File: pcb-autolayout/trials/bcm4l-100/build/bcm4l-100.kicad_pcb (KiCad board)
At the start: 4 copper layers, 80 x 60 mm, 120 parts, among them J1 MicroFit 2x4, J2 MicroFit 2x6, J3 SWD, Q1 SQD40P06 (P-MOS), Q11 AO3401A, Q12 MMBT3904, Q13 AO3401A, Q14 MMBT3904, Q15 AO3401A, Q16 MMBT3904, Q17 AO3401A, Q18 MMBT3904, SW1 RESET, U1 TPS54202, U2 AMS1117-3.3, U3 TJA1051T/3, U4 TJA1021T/20, U5 STM32F103C8T6, Y1 8MHz

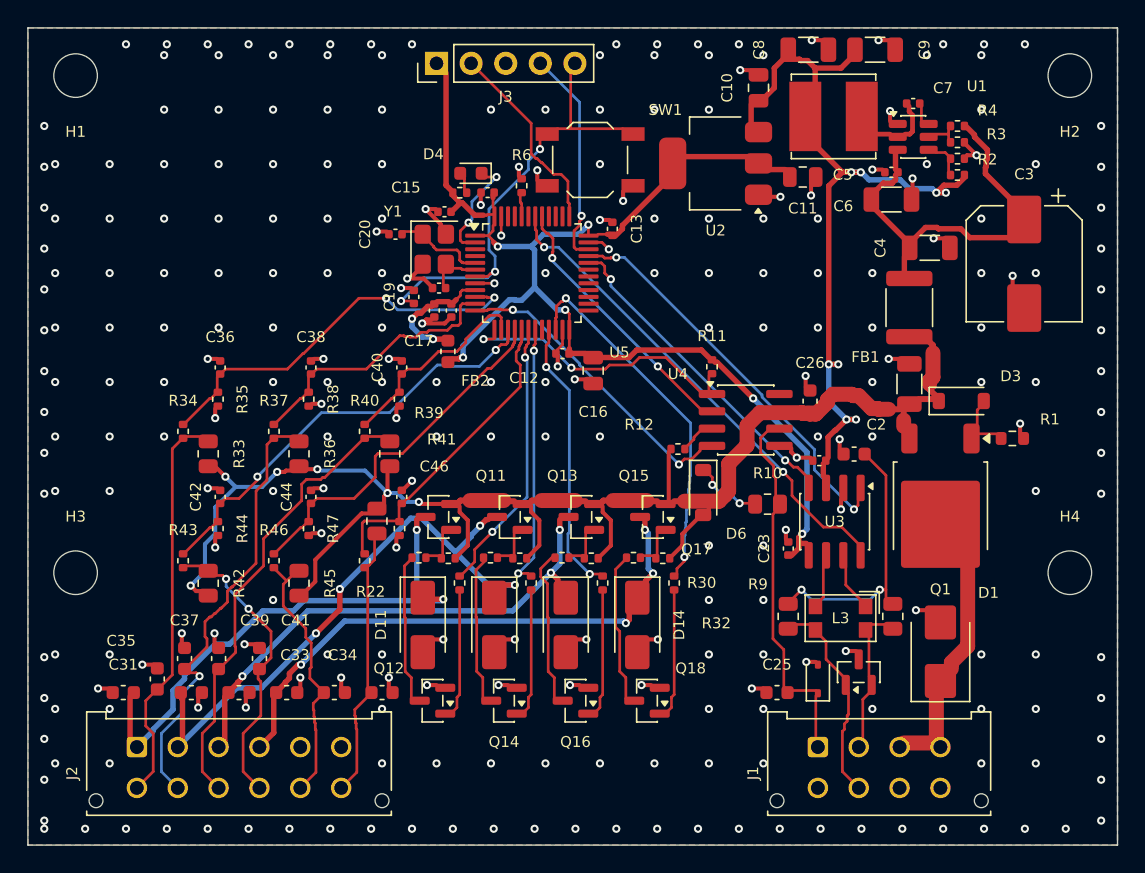
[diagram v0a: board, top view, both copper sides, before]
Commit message: A0: bench baseline đầu tiên (KiCad 9)
R: bcm4l-100 16/16 (343 s), synth-lo 16/16 (181 s), synth-hi 100 % chân nhưng DRC 21, RT-CLR.
V: 3 demo KiCad. Trial tổng hợp + build của chúng vào repo làm mốc.

Co-Authored-By: Claude Opus 5.5 <noreply@anthropic.com>
Claude-Session: https://claude.ai/code/session_012jwodCpQFB8wopi3P3TnUz
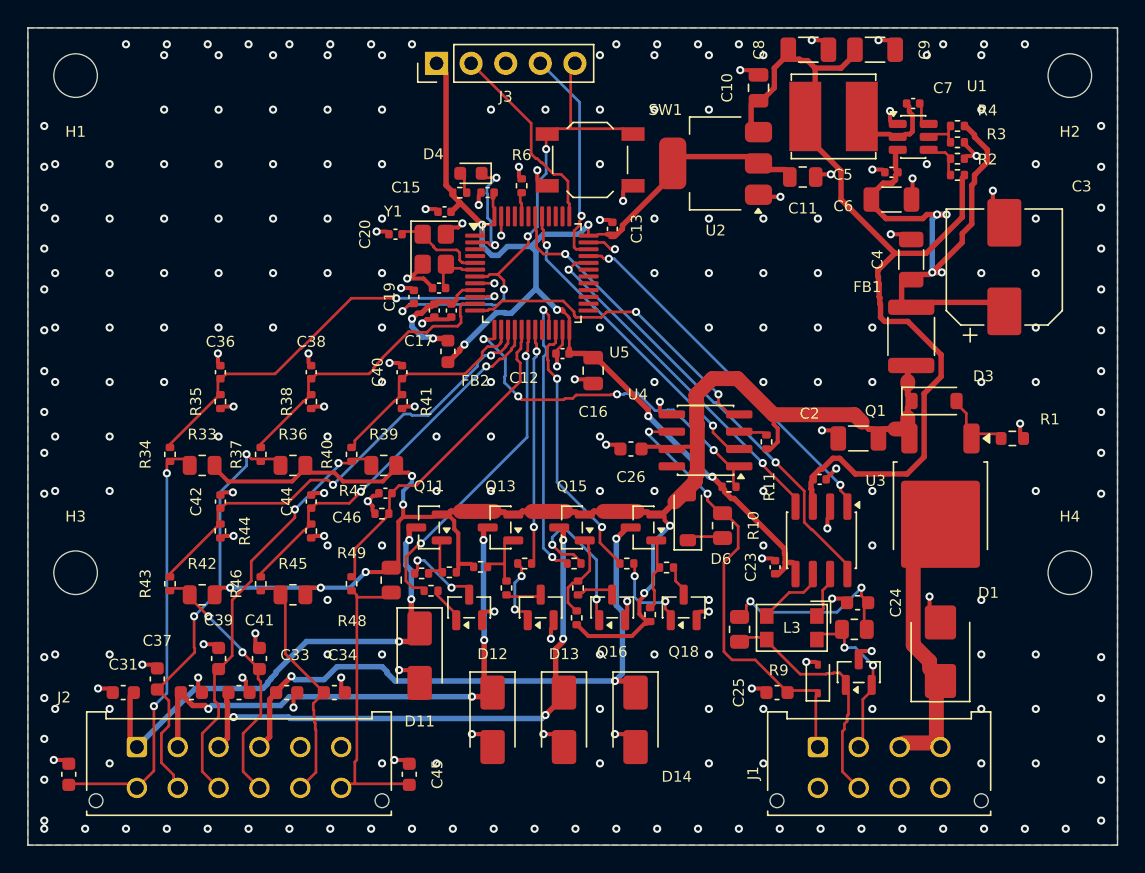
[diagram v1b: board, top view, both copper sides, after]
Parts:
- C2: renamed from C9; value 22u 10V -> 100n 50V
- C20: renamed from C40; value 10n -> 20p
- C25: renamed from C26; value 100n 50V -> 1n 50V
- C26: renamed from C25; value 1n 50V -> 100n 50V
- C46: renamed from C20; value 20p -> 10n
- C5: renamed from C2; value 100n 50V -> 10u 50V
- C9: renamed from C5; value 10u 50V -> 22u 10V
- Q11: renamed from Q12; value MMBT3904 -> AO3401A
- Q12: renamed from Q11; value AO3401A -> MMBT3904
- Q13: renamed from Q14; value MMBT3904 -> AO3401A
- Q14: renamed from Q13; value AO3401A -> MMBT3904
- Q15: renamed from Q16; value MMBT3904 -> AO3401A
- Q16: renamed from Q15; value AO3401A -> MMBT3904
- Q17: renamed from Q18; value MMBT3904 -> AO3401A
- Q18: renamed from Q17; value AO3401A -> MMBT3904
- R11: renamed from R12; value 10k -> 4k7
- R12: renamed from R11; value 4k7 -> 10k
- R21: renamed from R23; value 1k -> 10k
- R23: renamed from R21; value 10k -> 1k
- R28: renamed from R29; value 1k -> 10k
- R29: renamed from R28; value 10k -> 1k
- R31: renamed from R32; value 1k -> 10k
- R32: renamed from R31; value 10k -> 1k
- moved C2 28.6 mm to (161.0, 90.1), turned to 180 degrees
- moved C25 21.5 mm to (155.0, 108.8), turned to 180 degrees
- moved C26 20.9 mm to (144.3, 90.9)
- moved C46 19.0 mm to (126.2, 94.2)
- moved C5 13.6 mm to (163.4, 72.6), turned to 0 degrees
- moved Q11 12.7 mm to (129.4, 96.7)
- moved Q13 12.7 mm to (134.7, 96.7)
- moved Q15 12.7 mm to (139.9, 96.7)
- moved Q17 12.7 mm to (145.2, 96.7)
- moved R43 11.2 mm to (110.4, 100.8)
- moved R49 11.2 mm to (123.8, 100.8)
- moved R46 11.2 mm to (117.1, 100.8)
- moved C9 11.1 mm to (162.2, 61.6)
- moved C24 10.9 mm to (160.9, 102.2)
- moved C20 9.79 mm to (127.0, 75.2), turned to 180 degrees
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- renumbered C35 to C31, C31 to C35, C46 to C40, R25 to R24, R24 to R25, R43 to R34, R46 to R37, R48 to R39, R49 to R40, R50 to R41, R34 to R43, R37 to R46, R39 to R48, R40 to R49, R41 to R50
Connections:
- C2 pad 1: +5V -> VBAT_P
- C20 pad 1: IN3_M -> OSC_IN
- C25 pad 1: VBAT_P -> LIN
- C26 pad 1: LIN -> VBAT_P
- C31 pad 1: IN1 -> OUT1
- C35 pad 1: OUT1 -> IN1
- C40 pad 1: IN6_M -> IN3_M
- C46 pad 1: OSC_IN -> IN6_M
- C5 pad 1: VBAT_P -> VBAT_F
- C9 pad 1: VBAT_F -> +5V
- Q11 pad 1: OUT1_B -> OUT1_G
- Q11 pad 2: GND -> VBAT_P
- Q11 pad 3: OUT1_C -> OUT1
- Q12 pad 1: OUT1_G -> OUT1_B
- Q12 pad 2: VBAT_P -> GND
- Q12 pad 3: OUT1 -> OUT1_C
- Q13 pad 1: OUT2_B -> OUT2_G
- Q13 pad 2: GND -> VBAT_P
- Q13 pad 3: OUT2_C -> OUT2
- Q14 pad 1: OUT2_G -> OUT2_B
- Q14 pad 2: VBAT_P -> GND
- Q14 pad 3: OUT2 -> OUT2_C
- Q15 pad 1: OUT3_B -> OUT3_G
- Q15 pad 2: GND -> VBAT_P
- Q15 pad 3: OUT3_C -> OUT3
- Q16 pad 1: OUT3_G -> OUT3_B
- Q16 pad 2: VBAT_P -> GND
- Q16 pad 3: OUT3 -> OUT3_C
- Q17 pad 1: OUT4_B -> OUT4_G
- Q17 pad 2: GND -> VBAT_P
- Q17 pad 3: OUT4_C -> OUT4
- Q18 pad 1: OUT4_G -> OUT4_B
- Q18 pad 2: VBAT_P -> GND
- Q18 pad 3: OUT4 -> OUT4_C
- R11 pad 1: LIN_WAKE -> LIN_RX
- R11 pad 2: VBAT_P -> +3V3
- R12 pad 1: LIN_RX -> LIN_WAKE
- R12 pad 2: +3V3 -> VBAT_P
- R21 pad 1: OUT1_M -> VBAT_P
- R21 pad 2: OUT1_B -> OUT1_G
- R23 pad 1: VBAT_P -> OUT1_M
- R23 pad 2: OUT1_G -> OUT1_B
- R24 pad 1: OUT2_G -> VBAT_P
- R24 pad 2: OUT2_C -> OUT2_G
- R25 pad 1: VBAT_P -> OUT2_G
- R25 pad 2: OUT2_G -> OUT2_C
- R28 pad 1: OUT3_M -> OUT3_G
- R28 pad 2: OUT3_B -> OUT3_C
- R29 pad 1: OUT3_G -> OUT3_M
- R29 pad 2: OUT3_C -> OUT3_B
- R31 pad 1: OUT4_M -> OUT4_G
- R31 pad 2: OUT4_B -> OUT4_C
- R32 pad 1: OUT4_G -> OUT4_M
- R32 pad 2: OUT4_C -> OUT4_B
- R34 pad 1: IN4 -> IN1
- R34 pad 2: IN4_M -> IN1_M
- R37 pad 1: IN5 -> IN2
- R37 pad 2: IN5_M -> IN2_M
- R39 pad 2: IN6 -> IN3
- R40 pad 1: IN6 -> IN3
- R40 pad 2: IN6_M -> IN3_M
- R41 pad 1: IN6_M -> IN3_M
- R43 pad 1: IN1 -> IN4
- R43 pad 2: IN1_M -> IN4_M
- R46 pad 1: IN2 -> IN5
- R46 pad 2: IN2_M -> IN5_M
- R48 pad 2: IN3 -> IN6
- R49 pad 1: IN3 -> IN6
- R49 pad 2: IN3_M -> IN6_M
- R50 pad 1: IN3_M -> IN6_M
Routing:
- net VBAT_F: track 22.4 -> 35.1 mm, vias 0 -> 4
- net OUT4_C: track 10.7 -> 1.32 mm
- net OUT3_C: track 11.2 -> 2.18 mm
- net OUT2_C: track 10.6 -> 2.10 mm
- net OUT4_M: track 26.5 -> 18.9 mm
- net +5V: track 52.1 -> 59.2 mm, vias 8 -> 0
- net OUT1_B: track 8.89 -> 1.84 mm
- net CAN_SPL: track 18.6 -> 12.2 mm
- net LIN: track 24.0 -> 29.6 mm, vias 0 -> 2
- net OUT1_C: track 10.5 -> 5.24 mm, vias 0 -> 2
- net LIN_RX: track 20.0 -> 25.1 mm, vias 2 -> 4
- net OUT1: track 37.4 -> 32.6 mm, vias 2 -> 3
- net OUT2: track 42.0 -> 37.2 mm
- net OUT2_B: track 8.89 -> 4.21 mm, vias 0 -> 2
- net OUT4: track 37.7 -> 42.4 mm, vias 4 -> 3
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
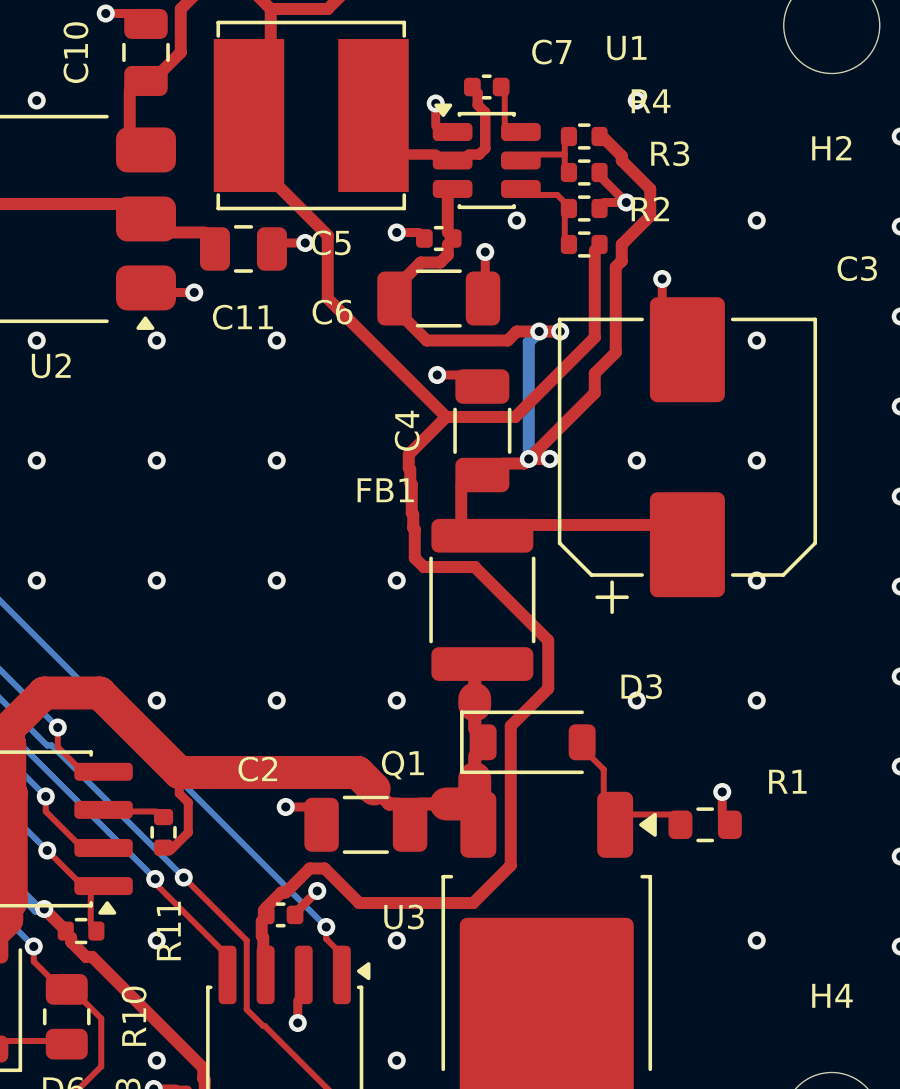
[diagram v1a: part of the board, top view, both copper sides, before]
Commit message: Engine 6 lớp + trial BCM-6L (239 linh kiện); sửa placer kéo đích vào vùng
- router: số lớp đi dây theo stackup.routing; pad SMD F/B -> lớp 0 / L-1, pad xuyên lỗ mọi lớp
- kicad_board: N lớp đồng, zone theo stackup.planes, _layer_id theo tên
- render: màu theo tên lớp
- placer: đích ngoài vùng kéo về điểm gần nhất trong vùng (sau khi nới vùng decap/near):
  xoắn ốc chỉ quét 40 mm — Q27 có 4284 chỗ trống trong vùng mà vẫn 'hết chỗ'
- trials/bcm6l-240: mạch luyện BCM 6 lớp (MCU LQFP-64, 2 CAN, 2 LIN, 8 HS, 4 LS, 12 DIN, 4 AIN),
  floorplan SIG/GND/SIG/SIG/GND/SIG; placement đạt mọi rule PLC
- bcm4l-100 hồi quy 4 lớp: 16/16

Co-Authored-By: Claude Opus 5.5 <noreply@anthropic.com>
Claude-Session: https://claude.ai/code/session_012jwodCpQFB8wopi3P3TnUz
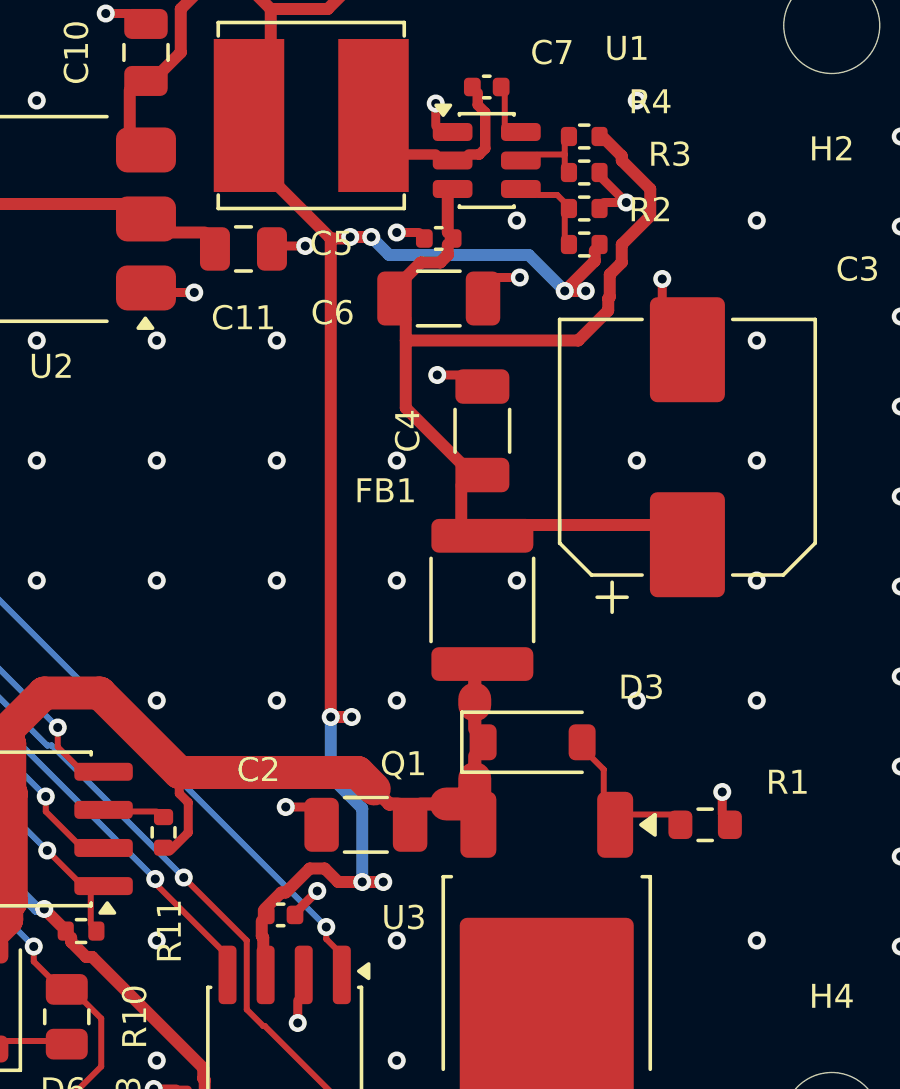
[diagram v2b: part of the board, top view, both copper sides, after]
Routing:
- net VBAT_F: track 35.1 -> 28.8 mm, vias 4 -> 0
- net +5V: track 59.2 -> 55.9 mm, vias 0 -> 8
- net GND: vias 267 -> 269
